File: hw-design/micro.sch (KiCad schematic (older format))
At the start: 34 parts, among them P1 test-double, P2 CONN_01X04, P6 CONN_01X05, P7 CONN_01X05, U1 STM32F072CB/F042C6, U2 usb-micro, Y1 16MHz

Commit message: 3 boards split
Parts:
- removed C2, C3: 10pF, w_smd_cap:c_0603, symbol C
- removed D1, D2, D3, D4: LED, LEDs:LED_0603, symbol LED
- removed P1: test-double, iwasz:testpad-2p, symbol test-double
- removed P2: CONN_01X04, w_pin_strip:pin_strip_4, symbol CONN_01X04
- removed P6, P7: CONN_01X05, w_pin_strip:pin_strip_5, symbol CONN_01X05
- removed R1, R2, R3, R4: 680R, w_smd_resistors:r_0603, symbol R
- removed R10, R11, R8, R9: 22R, w_smd_resistors:r_0603, symbol R
- removed R6: 220R, w_smd_resistors:r_0603, symbol R
- removed U1: STM32F072CB/F042C6, w_smd_lqfp:lqfp48, symbol STM32F0-LQFP48
- removed U2: usb-micro, w_conn_pc:conn_usb_B_micro_smd-2, symbol usb-micro
- added C39, C40: 15pF, w_smd_cap:c_0603, symbol C
- added R34: 220, w_smd_resistors:r_0402, symbol R
- added U14: STM32F030CxTx, w_smd_lqfp:lqfp48, symbol STM32F030CxTx
- R5, R7: footprint w_smd_resistors:r_0603 -> w_smd_resistors:r_0402
- Y1: Opis (none) -> Kryształ 16MHz do radia do nRF8001
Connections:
- net labels added: console_rx, console_tx, ir_cannon, ir_sense, led_b, led_g, led_r, nrst, pb14, pb15, pc13, pc14, pc15, photo_illumination, photo_l_int, photo_r_int, scl, sda, sound
- net labels removed: +5V, head1, head2, led1, led2, led3, led4
- wire segments 117 -> 84
- no-connect marks 4 -> 1
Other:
- note added: "C6Tx : 32/4\nC8Tx : 64/8\nCCTx : 256/32"
- note added: "Crystal is optional"
- note added: "TODO Czy nie da się wszystkich IR sensorów podłączyć do jednego wejścia!?"
- note added: "TODO LED RGB"
- note added: "TODO Skalowalność µC - chodzi mi o pamięć flash i RAM"
- note added: "TODO Ustalić jaki w końcu ten mikrokontroler."
- note added: "TODO Włączniczek zamiast pinów"
- note added: "TODO dać USB, bo to umożliwi stosowanie płytki głównej\njako development boarda (głównie dla mnie?)."
- note added: "TODO dźwięk!"
- note added: "TODO serial console"
- moved on the sheet: C11, C12, R5, R7

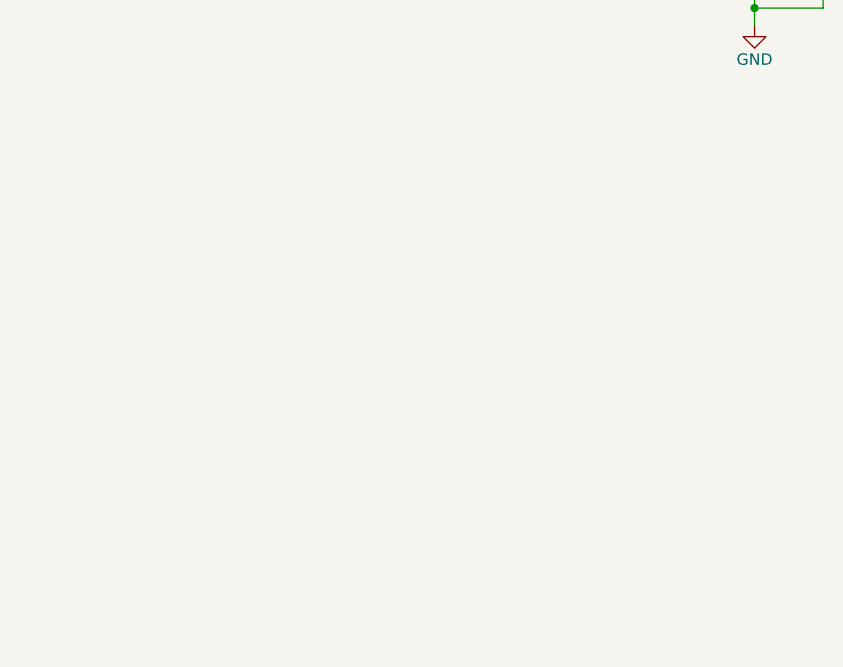
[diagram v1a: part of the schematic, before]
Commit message: Changed to 2 boards layout. On the top one there is only : speaker, IR stuff, RGB led.
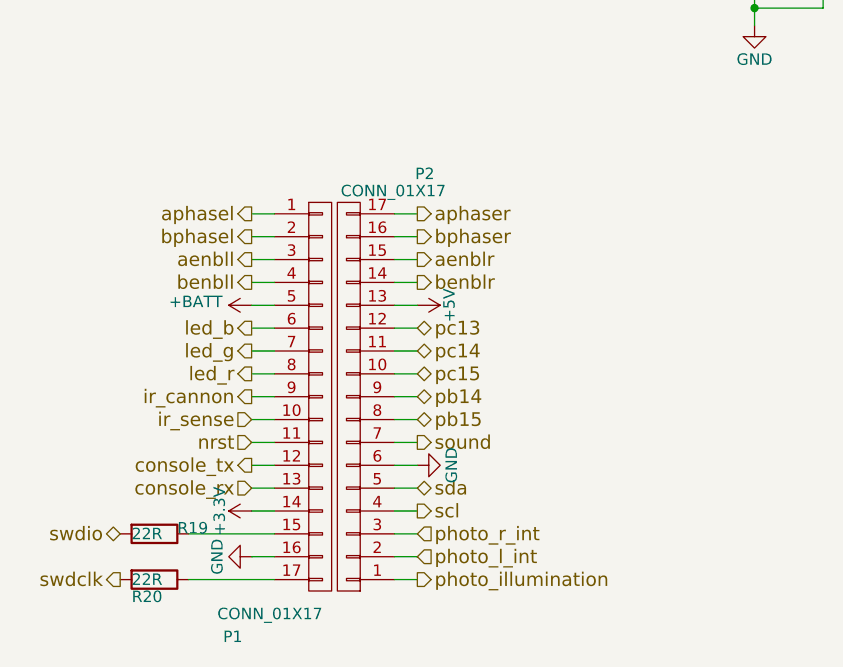
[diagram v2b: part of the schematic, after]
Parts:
- added P1, P2: CONN_01X17, w_pin_strip:pin_strip_17, symbol CONN_01X17
- added R19, R20: 22R, w_smd_resistors:r_0402, symbol R
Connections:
- net +3V3: now also P1.14 (P14)
- net GND: now also P1.16 (P16), P2.6 (P6)
- net aenbll: now also P1.3 (P3)
- net aenblr: now also P2.15 (P15)
- net aphasel: now also P1.1 (P1)
- net aphaser: now also P2.17 (P17)
- net benbll: now also P1.4 (P4)
- net benblr: now also P2.14 (P14)
- net bphasel: now also P1.2 (P2)
- net bphaser: now also P2.16 (P16)
- net console_rx: now also P1.13 (P13)
- net console_tx: now also P1.12 (P12)
- net ir_cannon: now also P1.9 (P9)
- net ir_sense: now also P1.10 (P10)
- net led_b: now also P1.6 (P6)
- net led_g: now also P1.7 (P7)
- net led_r: now also P1.8 (P8)
- net nrst: now also P1.11 (P11)
- net pb14: now also P2.9 (P9)
- net pb15: now also P2.8 (P8)
- net pc13: now also P2.12 (P12)
- net pc14: now also P2.11 (P11)
- net pc15: now also P2.10 (P10)
- net photo_illumination: now also P2.1 (P1)
- net photo_l_int: now also P2.2 (P2)
- net photo_r_int: now also P2.3 (P3)
- net scl: now also P2.4 (P4)
- net sda: now also P2.5 (P5)
- net sound: now also P2.7 (P7)
- net swdclk: now also R20.2
- net swdio: now also R19.2
- new net: P1.15 (P15), R19.1
- new net: P1.17 (P17), R20.1
- new net +5V: P2.13 (P13)
- new net +BATT: P1.5 (P5)

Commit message: Another idea of PCB split.
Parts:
- P1, P2: footprint w_pin_strip:pin_strip_17 -> iwasz:pin_socket_17
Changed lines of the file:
@@
 $Descr A4 11693 8268
 encoding utf-8
-Sheet 5 6
+Sheet 5 7
 Title ""
 Date ""
@@
 $EndComp
 $Comp
-L GND #PWR52
+L GND #PWR45
 U 1 1 5724042E
 P 4425 3025
-F 0 "#PWR52" H 4425 2775 50  0001 C CNN
+F 0 "#PWR45" H 4425 2775 50  0001 C CNN
 F 1 "GND" H 4425 2875 50  0000 C CNN
 F 2 "" H 4425 3025 60  0000 C CNN
@@
 $EndComp
 $Comp
-L GND #PWR56
+L GND #PWR49
 U 1 1 57240432
 P 7300 5750
-F 0 "#PWR56" H 7300 5500 50  0001 C CNN
+F 0 "#PWR49" H 7300 5500 50  0001 C CNN
 F 1 "GND" H 7300 5600 50  0000 C CNN
 F 2 "" H 7300 5750 60  0000 C CNN
@@
 $EndComp
 $Comp
-L GND #PWR55
+L GND #PWR48
 U 1 1 57240436
 P 5975 1500
-F 0 "#PWR55" H 5975 1250 50  0001 C CNN
+F 0 "#PWR48" H 5975 1250 50  0001 C CNN
 F 1 "GND" H 5975 1350 50  0000 C CNN
 F 2 "" H 5975 1500 60  0000 C CNN
@@
 $EndComp
 $Comp
-L GND #PWR50
+L GND #PWR43
 U 1 1 57240439
 P 3875 4775
-F 0 "#PWR50" H 3875 4525 50  0001 C CNN
+F 0 "#PWR43" H 3875 4525 50  0001 C CNN
 F 1 "GND" H 3875 4625 50  0000 C CNN
 F 2 "" H 3875 4775 60  0000 C CNN
@@
 $EndComp
 $Comp
-L GND #PWR53
+L GND #PWR46
 U 1 1 5724043A
 P 4750 4200
-F 0 "#PWR53" H 4750 3950 50  0001 C CNN
+F 0 "#PWR46" H 4750 3950 50  0001 C CNN
 F 1 "GND" H 4750 4050 50  0000 C CNN
 F 2 "" H 4750 4200 60  0000 C CNN
@@
 $EndComp
 $Comp
-L +3.3V #PWR54
+L +3.3V #PWR47
 U 1 1 57240443
 P 5450 1400
-F 0 "#PWR54" H 5450 1250 50  0001 C CNN
+F 0 "#PWR47" H 5450 1250 50  0001 C CNN
 F 1 "+3.3V" H 5450 1540 50  0000 C CNN
 F 2 "" H 5450 1400 60  0000 C CNN
@@
 $EndComp
 $Comp
-L +3.3V #PWR51
+L +3.3V #PWR44
 U 1 1 57240444
 P 4275 3500
-F 0 "#PWR51" H 4275 3350 50  0001 C CNN
+F 0 "#PWR44" H 4275 3350 50  0001 C CNN
 F 1 "+3.3V" H 4275 3640 50  0000 C CNN
 F 2 "" H 4275 3500 60  0000 C CNN
@@
 $EndComp
 $Comp
-L +3.3V #PWR57
+L +3.3V #PWR50
 U 1 1 57240445
 P 7450 5175
-F 0 "#PWR57" H 7450 5025 50  0001 C CNN
+F 0 "#PWR50" H 7450 5025 50  0001 C CNN
 F 1 "+3.3V" H 7450 5315 50  0000 C CNN
 F 2 "" H 7450 5175 60  0000 C CNN
@@
 $EndComp
 $Comp
-L +3.3V #PWR49
+L +3.3V #PWR42
 U 1 1 57240446
 P 3725 4300
-F 0 "#PWR49" H 3725 4150 50  0001 C CNN
+F 0 "#PWR42" H 3725 4150 50  0001 C CNN
 F 1 "+3.3V" H 3725 4440 50  0000 C CNN
 F 2 "" H 3725 4300 60  0000 C CNN
@@
 $EndComp
 $Comp
-L GND #PWR58
+L GND #PWR51
 U 1 1 5727D3BA
 P 8050 3675
-F 0 "#PWR58" H 8050 3425 50  0001 C CNN
+F 0 "#PWR51" H 8050 3425 50  0001 C CNN
 F 1 "GND" V 8055 3547 50  0000 R CNN
 F 2 "" H 8050 3675 50  0000 C CNN
@@
 	3200 3475 3000 3475
 $Comp
-L GND #PWR47
+L GND #PWR40
 U 1 1 580B1D68
 P 3000 3475
-F 0 "#PWR47" H 3000 3225 50  0001 C CNN
+F 0 "#PWR40" H 3000 3225 50  0001 C CNN
 F 1 "GND" H 3000 3325 50  0000 C CNN
 F 2 "" H 3000 3475 60  0000 C CNN
@@
 $EndComp
 $Comp
-L GND #PWR48
+L GND #PWR41
 U 1 1 580B1D6E
 P 3000 4000
-F 0 "#PWR48" H 3000 3750 50  0001 C CNN
+F 0 "#PWR41" H 3000 3750 50  0001 C CNN
 F 1 "GND" H 3000 3850 50  0000 C CNN
 F 2 "" H 3000 4000 60  0000 C CNN
@@
 $EndComp
 $Comp
-L GND #PWR44
+L GND #PWR37
 U 1 1 58152F0B
 P 1675 7100
-F 0 "#PWR44" H 1675 6850 50  0001 C CNN
+F 0 "#PWR37" H 1675 6850 50  0001 C CNN
 F 1 "GND" H 1675 6950 50  0000 C CNN
 F 2 "" H 1675 7100 60  0000 C CNN
@@
 $EndComp
 $Comp
-L +3.3V #PWR43
+L +3.3V #PWR36
 U 1 1 58152F11
 P 1675 6900
-F 0 "#PWR43" H 1675 6750 50  0001 C CNN
+F 0 "#PWR36" H 1675 6750 50  0001 C CNN
 F 1 "+3.3V" H 1675 7040 50  0000 C CNN
 F 2 "" H 1675 6900 60  0000 C CNN
@@
 $EndComp
 $Comp
-L +BATT #PWR42
+L +BATT #PWR35
 U 1 1 58152F17
 P 1675 6000
-F 0 "#PWR42" H 1675 5850 50  0001 C CNN
+F 0 "#PWR35" H 1675 5850 50  0001 C CNN
 F 1 "+BATT" V 1690 6127 50  0000 L CNN
 F 2 "" H 1675 6000 50  0000 C CNN
@@
 $EndComp
 $Comp
-L +5V #PWR45
+L +5V #PWR38
 U 1 1 58152F1D
 P 2400 6000
-F 0 "#PWR45" H 2400 5850 50  0001 C CNN
+F 0 "#PWR38" H 2400 5850 50  0001 C CNN
 F 1 "+5V" H 2400 6140 50  0000 C CNN
 F 2 "" H 2400 6000 60  0000 C CNN
@@
 F 0 "P1" H 1550 5350 50  0000 L CNN
 F 1 "CONN_01X17" H 1525 5450 50  0000 L CNN
-F 2 "w_pin_strip:pin_strip_17" H 1975 6400 50  0001 C CNN
+F 2 "iwasz:pin_socket_17" H 1975 6400 50  0001 C CNN
 F 3 "" H 1975 6400 50  0000 C CNN
 	1    1975 6400
@@
 F 0 "P2" H 1725 5425 50  0000 L CNN
 F 1 "CONN_01X17" H 1675 5500 50  0000 L CNN
-F 2 "w_pin_strip:pin_strip_17" H 2100 6400 50  0001 C CNN
+F 2 "iwasz:pin_socket_17" H 2100 6400 50  0001 C CNN
 F 3 "" H 2100 6400 50  0000 C CNN
 	1    2100 6400
@@
 $EndComp
 $Comp
-L GND #PWR46
+L GND #PWR39
 U 1 1 58152F31
 P 2400 6700
-F 0 "#PWR46" H 2400 6450 50  0001 C CNN
+F 0 "#PWR39" H 2400 6450 50  0001 C CNN
 F 1 "GND" H 2400 6550 50  0000 C CNN
 F 2 "" H 2400 6700 60  0000 C CNN

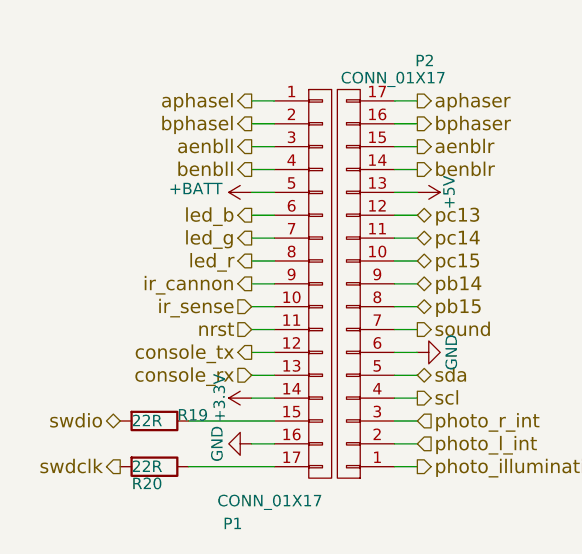
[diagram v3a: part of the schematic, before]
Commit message: 2 boards and 1 little with color sensors.
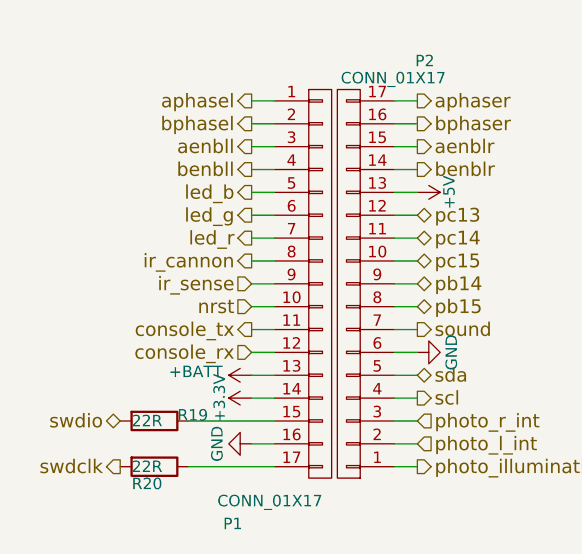
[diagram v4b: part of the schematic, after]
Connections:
- net +BATT: now also P1.13 (P13); no longer P1.5 (P5)
- net console_rx: now also P1.12 (P12); no longer P1.13 (P13)
- net console_tx: now also P1.11 (P11); no longer P1.12 (P12)
- net ir_cannon: now also P1.8 (P8); no longer P1.9 (P9)
- net ir_sense: now also P1.9 (P9); no longer P1.10 (P10)
- net led_b: now also P1.5 (P5); no longer P1.6 (P6)
- net led_g: now also P1.6 (P6); no longer P1.7 (P7)
- net led_r: now also P1.7 (P7); no longer P1.8 (P8)
- net nrst: now also P1.10 (P10); no longer P1.11 (P11)
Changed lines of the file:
@@
 $EndComp
 $Comp
-L GND #PWR45
+L GND #PWR035
 U 1 1 5724042E
 P 4425 3025
-F 0 "#PWR45" H 4425 2775 50  0001 C CNN
+F 0 "#PWR035" H 4425 2775 50  0001 C CNN
 F 1 "GND" H 4425 2875 50  0000 C CNN
 F 2 "" H 4425 3025 60  0000 C CNN
@@
 $EndComp
 $Comp
-L GND #PWR49
+L GND #PWR036
 U 1 1 57240432
 P 7300 5750
-F 0 "#PWR49" H 7300 5500 50  0001 C CNN
+F 0 "#PWR036" H 7300 5500 50  0001 C CNN
 F 1 "GND" H 7300 5600 50  0000 C CNN
 F 2 "" H 7300 5750 60  0000 C CNN
@@
 $EndComp
 $Comp
-L GND #PWR48
+L GND #PWR037
 U 1 1 57240436
 P 5975 1500
-F 0 "#PWR48" H 5975 1250 50  0001 C CNN
+F 0 "#PWR037" H 5975 1250 50  0001 C CNN
 F 1 "GND" H 5975 1350 50  0000 C CNN
 F 2 "" H 5975 1500 60  0000 C CNN
@@
 $EndComp
 $Comp
-L GND #PWR43
+L GND #PWR038
 U 1 1 57240439
 P 3875 4775
-F 0 "#PWR43" H 3875 4525 50  0001 C CNN
+F 0 "#PWR038" H 3875 4525 50  0001 C CNN
 F 1 "GND" H 3875 4625 50  0000 C CNN
 F 2 "" H 3875 4775 60  0000 C CNN
@@
 $EndComp
 $Comp
-L GND #PWR46
+L GND #PWR039
 U 1 1 5724043A
 P 4750 4200
-F 0 "#PWR46" H 4750 3950 50  0001 C CNN
+F 0 "#PWR039" H 4750 3950 50  0001 C CNN
 F 1 "GND" H 4750 4050 50  0000 C CNN
 F 2 "" H 4750 4200 60  0000 C CNN
@@
 $EndComp
 $Comp
-L +3.3V #PWR47
+L +3.3V #PWR040
 U 1 1 57240443
 P 5450 1400
-F 0 "#PWR47" H 5450 1250 50  0001 C CNN
+F 0 "#PWR040" H 5450 1250 50  0001 C CNN
 F 1 "+3.3V" H 5450 1540 50  0000 C CNN
 F 2 "" H 5450 1400 60  0000 C CNN
@@
 $EndComp
 $Comp
-L +3.3V #PWR44
+L +3.3V #PWR041
 U 1 1 57240444
 P 4275 3500
-F 0 "#PWR44" H 4275 3350 50  0001 C CNN
+F 0 "#PWR041" H 4275 3350 50  0001 C CNN
 F 1 "+3.3V" H 4275 3640 50  0000 C CNN
 F 2 "" H 4275 3500 60  0000 C CNN
@@
 $EndComp
 $Comp
-L +3.3V #PWR50
+L +3.3V #PWR042
 U 1 1 57240445
 P 7450 5175
-F 0 "#PWR50" H 7450 5025 50  0001 C CNN
+F 0 "#PWR042" H 7450 5025 50  0001 C CNN
 F 1 "+3.3V" H 7450 5315 50  0000 C CNN
 F 2 "" H 7450 5175 60  0000 C CNN
@@
 $EndComp
 $Comp
-L +3.3V #PWR42
+L +3.3V #PWR043
 U 1 1 57240446
 P 3725 4300
-F 0 "#PWR42" H 3725 4150 50  0001 C CNN
+F 0 "#PWR043" H 3725 4150 50  0001 C CNN
 F 1 "+3.3V" H 3725 4440 50  0000 C CNN
 F 2 "" H 3725 4300 60  0000 C CNN
@@
 $EndComp
 $Comp
-L GND #PWR51
+L GND #PWR044
 U 1 1 5727D3BA
 P 8050 3675
-F 0 "#PWR51" H 8050 3425 50  0001 C CNN
+F 0 "#PWR044" H 8050 3425 50  0001 C CNN
 F 1 "GND" V 8055 3547 50  0000 R CNN
 F 2 "" H 8050 3675 50  0000 C CNN
@@
 	3200 3475 3000 3475
 $Comp
-L GND #PWR40
+L GND #PWR045
 U 1 1 580B1D68
 P 3000 3475
-F 0 "#PWR40" H 3000 3225 50  0001 C CNN
+F 0 "#PWR045" H 3000 3225 50  0001 C CNN
 F 1 "GND" H 3000 3325 50  0000 C CNN
 F 2 "" H 3000 3475 60  0000 C CNN
@@
 $EndComp
 $Comp
-L GND #PWR41
+L GND #PWR046
 U 1 1 580B1D6E
 P 3000 4000
-F 0 "#PWR41" H 3000 3750 50  0001 C CNN
+F 0 "#PWR046" H 3000 3750 50  0001 C CNN
 F 1 "GND" H 3000 3850 50  0000 C CNN
 F 2 "" H 3000 4000 60  0000 C CNN
@@
 $EndComp
 $Comp
-L GND #PWR37
+L GND #PWR047
 U 1 1 58152F0B
 P 1675 7100
-F 0 "#PWR37" H 1675 6850 50  0001 C CNN
+F 0 "#PWR047" H 1675 6850 50  0001 C CNN
 F 1 "GND" H 1675 6950 50  0000 C CNN
 F 2 "" H 1675 7100 60  0000 C CNN
@@
 $EndComp
 $Comp
-L +3.3V #PWR36
+L +3.3V #PWR048
 U 1 1 58152F11
 P 1675 6900
-F 0 "#PWR36" H 1675 6750 50  0001 C CNN
+F 0 "#PWR048" H 1675 6750 50  0001 C CNN
 F 1 "+3.3V" H 1675 7040 50  0000 C CNN
 F 2 "" H 1675 6900 60  0000 C CNN
@@
 $EndComp
 $Comp
-L +BATT #PWR35
+L +BATT #PWR049
 U 1 1 58152F17
-P 1675 6000
-F 0 "#PWR35" H 1675 5850 50  0001 C CNN
-F 1 "+BATT" V 1690 6127 50  0000 L CNN
-F 2 "" H 1675 6000 50  0000 C CNN
-F 3 "" H 1675 6000 50  0000 C CNN
-	1    1675 6000
-	0    -1   -1   0
-$EndComp
-$Comp
-L +5V #PWR38
+P 1675 6800
+F 0 "#PWR049" H 1675 6650 50  0001 C CNN
+F 1 "+BATT" V 1690 6927 50  0000 L CNN
+F 2 "" H 1675 6800 50  0000 C CNN
+F 3 "" H 1675 6800 50  0000 C CNN
+	1    1675 6800
+	0    -1   -1   0
+$EndComp
+$Comp
+L +5V #PWR050
 U 1 1 58152F1D
 P 2400 6000
-F 0 "#PWR38" H 2400 5850 50  0001 C CNN
+F 0 "#PWR050" H 2400 5850 50  0001 C CNN
 F 1 "+5V" H 2400 6140 50  0000 C CNN
 F 2 "" H 2400 6000 60  0000 C CNN
@@
 $EndComp
 $Comp
-L GND #PWR39
+L GND #PWR051
 U 1 1 58152F31
 P 2400 6700
-F 0 "#PWR39" H 2400 6450 50  0001 C CNN
+F 0 "#PWR051" H 2400 6450 50  0001 C CNN
 F 1 "GND" H 2400 6550 50  0000 C CNN
 F 2 "" H 2400 6700 60  0000 C CNN
@@
 Text HLabel 1675 5900 0    60   Output ~ 0
 benbll
+Text HLabel 1675 6000 0    60   Output ~ 0
+led_b
 Text HLabel 1675 6100 0    60   Output ~ 0
-led_b
+led_g
 Text HLabel 1675 6200 0    60   Output ~ 0
-led_g
+led_r
 Text HLabel 1675 6300 0    60   Output ~ 0
-led_r
-Text HLabel 1675 6400 0    60   Output ~ 0
 ir_cannon
+Text HLabel 1675 6400 0    60   Input ~ 0
+ir_sense
 Text HLabel 1675 6500 0    60   Input ~ 0
-ir_sense
-Text HLabel 1675 6600 0    60   Input ~ 0
 nrst
-Text HLabel 1675 6700 0    60   Output ~ 0
+Text HLabel 1675 6600 0    60   Output ~ 0
 console_tx
-Text HLabel 1675 6800 0    60   Input ~ 0
+Text HLabel 1675 6700 0    60   Input ~ 0
 console_rx
 Text HLabel 1100 7000 0    60   BiDi ~ 0
